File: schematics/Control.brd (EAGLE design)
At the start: 100 x 99.8 mm, 57 parts, among them IC1 THAT1646, IC2 THAT1646, IC5 NE5532N

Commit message: rev01 for pcbtrain express fab
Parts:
- removed BOOT, BOOT1, JP4: (no value), SparkFun:1X03
- removed C501, C502: 2n7 C0G, Rebel:C0603
- removed C503, C504: 100n, Rebel:C0603
- removed JP2: (no value), SparkFun:1X02
- added C10, C300, C301, C9: 0.1uF, capacitor-wima:C5B3.5
- added C11, C12, C610: 100n, rcl:C050-025X075
- added C13, C14: 2n7 C0G, rcl:C050-025X075
- added C15, C16, C611: 100uF, rcl:E2,5-7
- added IN2: (no value), SparkFun:1X02
- added J4, J5: NEUTRIK_NMJ6HCD2, neutrik_jacks:NMJ6HCD2
- added JP13: (no value), SparkFun:1X05
- added R1, R2, R3, R4, R5: 91R, Rebel:0204/7
- added R300, R301: 2M, Rebel:0204/7
- added U$1, U$3, U$4, U$5, U$6: (no value), holes:2,8
- added UART: (no value), SparkFun:1X03
- JP1: device SparkFun:1X02 -> SparkFun:1X05
- R501, R502, R503, R504, R505, R506, R507, R508, R509, R510: device Rebel:0603 -> Rebel:0204/7
- moved C7 210.8 mm to (97.8, 62.2), turned to 180 degrees
- moved RIGHT 209.6 mm to (97.8, 102.9)
- moved C6 207.6 mm to (101.6, 52.1), turned to 90 degrees
- moved C8 203.8 mm to (88.9, 62.2), turned to 180 degrees
- moved C5 196.6 mm to (83.8, 44.5), turned to 270 degrees
- moved IC2 196.5 mm to (94.0, 50.8), turned to 270 degrees
- moved C1 187.5 mm to (101.6, 44.5), turned to 270 degrees
- moved C3 187.2 mm to (80.0, 62.2), turned to 180 degrees
- moved C4 182.4 mm to (71.1, 62.2)
- moved C2 182.1 mm to (83.8, 52.1), turned to 90 degrees
- moved LEFT 160.7 mm to (69.8, 102.9)
- moved IC1 139.4 mm to (76.2, 50.8), turned to 270 degrees
- moved IN1 131.7 mm to (2.86, 21.9), turned to 90 degrees
- moved VMID1 128.1 mm to (2.86, 27.0), turned to 180 degrees
- moved HP1 125.2 mm to (2.86, 32.1), turned to 270 degrees
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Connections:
- removed net +3V3: BOOT.3, BOOT1.3, JP3.3, JP4.3, JP5.3
- removed net AINA: C501.1, R503.2
- removed net AINB: C502.1, R508.2
- removed net BOOT0: BOOT.2, BOOT1.2, JP12.2, JP9.2
- removed net INL: R502.1
- removed net INR: R507.1
- removed net L_IN1: IN.1
- removed net L_IN2: IN1.1
- removed net L_OUT1: HP.2
- removed net L_OUT2: HP1.2
- removed net OUT_LEFT: IC1.4
- removed net OUT_RIGHT: IC2.4
- removed net R_IN1: IN.2
- removed net R_IN2: IN1.2
- removed net R_OUT1: HP.1
- removed net R_OUT2: HP1.1
- removed net USB_VBUS: JP1.2, JP2.2, USB.4, USB1.4
- new net ADC1_A: ADC.4
- new net ADC2_A: ADC.3
- new net ADC3_A: ADC.2
- new net ADC4_A: ADC.1
- new net FX_IN_L: C300.2, J4.T, J5.TN, R300.2
- new net FX_IN_R: C301.2, J5.T, R301.2
- new net L_IN_A: IN.1, R1.1
- new net L_IN_B: C13.1, IN1.1, R503.2
- new net L_OUT_A: C10.2, HP.2
- new net L_OUT_B: HP1.2, R1.2
- new net N$26: C300.1, R502.1
- new net N$30: C301.1, R507.1
- new net N$7: C9.1, IC2.4
- new net N$9: C10.1, IC1.4
- new net PA2_A: JP7.2
- new net PA3_A: JP7.1
- new net PB6_A: JP9.4
- new net PB7_A: JP9.3
- new net PE2_A: JP10.4
- new net PE3_A: JP10.3
- new net PE4_A: JP10.2
- new net PE5_A: JP10.1
- new net PG14_A: JP9.1
- new net RX: R3.1, UART.3
- new net RX_A: JP13.2, R5.1
- new net RX_B: JP1.2, R3.2
- new net R_IN_A: IN.2, R2.1
- new net R_IN_B: C14.1, IN1.2, R508.2
- new net R_OUT_A: C9.2, HP.1
- new net R_OUT_B: HP1.1, R2.2
- new net TX: R4.1, UART.1
- new net TX_A: JP13.3, R4.2
- new net TX_B: JP1.3, R5.2
- new net USB_DM_A: USB.3
- new net USB_DP_A: USB.2
- new net USB_ID_A: USB.1
- net +12V: now also C11.1; no longer C503.1
- net +5V: now also C15.+, C16.+; no longer JP1.1, JP2.1, JP4.1
- net -12V: now also C12.1; no longer C504.1
- net ADC1: no longer ADC.4
- net ADC2: no longer ADC.3
- net ADC3: no longer ADC.2
- net ADC4: no longer ADC.1
- net CS_VREF: now also C13.2, C14.2, C610.1, C611.+, VMID1.1; no longer C501.2, C502.2
- net GND: now also C11.2, C12.2, C15.-, C16.-, C610.2, C611.-, IN2.2, J4.S, J4.TN, J5.S, JP12.2, JP9.2, R300.1, R301.1, UART.2; no longer BOOT.1, BOOT1.1, C503.2, C504.2, JP4.2
- net GNDA: now also IN2.1
- net PA2: no longer JP7.2
- net PA3: no longer JP7.1
- net PB6: no longer JP9.4
- net PB7: no longer JP9.3
- net PE2: no longer JP10.4
- net PE3: no longer JP10.3
- net PE4: no longer JP10.2
- net PE5: no longer JP10.1
- net PG14: no longer JP9.1
- net USB_DM: no longer USB.3
- net USB_DP: no longer USB.2
- net USB_ID: no longer USB.1
- net VCC/2: no longer VMID1.1
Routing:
- net +5V: track 0.00 -> 183.9 mm, vias 0 -> 1
- net +12V: track 0.00 -> 104.5 mm
- net -12V: track 0.00 -> 102.7 mm, vias 0 -> 1
- net TX_A: track 0.00 -> 85.2 mm
- net CS_VREF: track 0.00 -> 84.1 mm, vias 0 -> 3
- net RX_A: track 0.00 -> 72.5 mm
- net R_IN_B: track 0.00 -> 67.0 mm, vias 0 -> 1
- net FX_IN_L: track 0.00 -> 58.9 mm
- net N$3: track 0.00 -> 55.1 mm
- net TX: track 0.00 -> 46.5 mm
- net RX: track 0.00 -> 46.5 mm
- net N$2: track 0.00 -> 44.8 mm
- net L_IN_B: track 0.00 -> 43.0 mm, vias 0 -> 1
- net R_IN_A: track 0.00 -> 42.9 mm
- net N$19: track 0.00 -> 42.9 mm
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- added copper zone on layer 16, net GNDA
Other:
- board size 100 x 99.8 mm -> 115.3 x 90.9 mm
- board text added: "OWL Rack Rev01"
- board text removed: "OWL Modular Rev02"

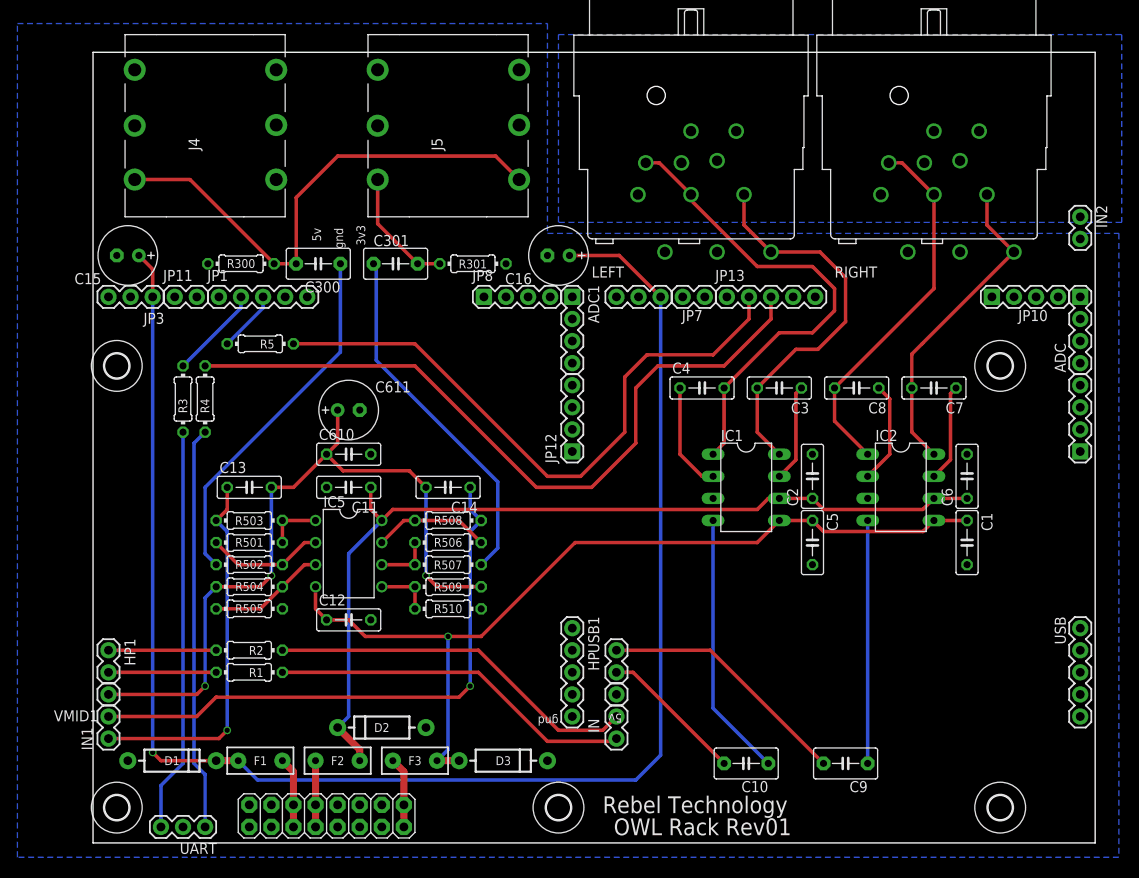
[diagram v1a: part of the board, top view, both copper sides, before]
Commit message: added +5v reg, change power connection, reduced board size
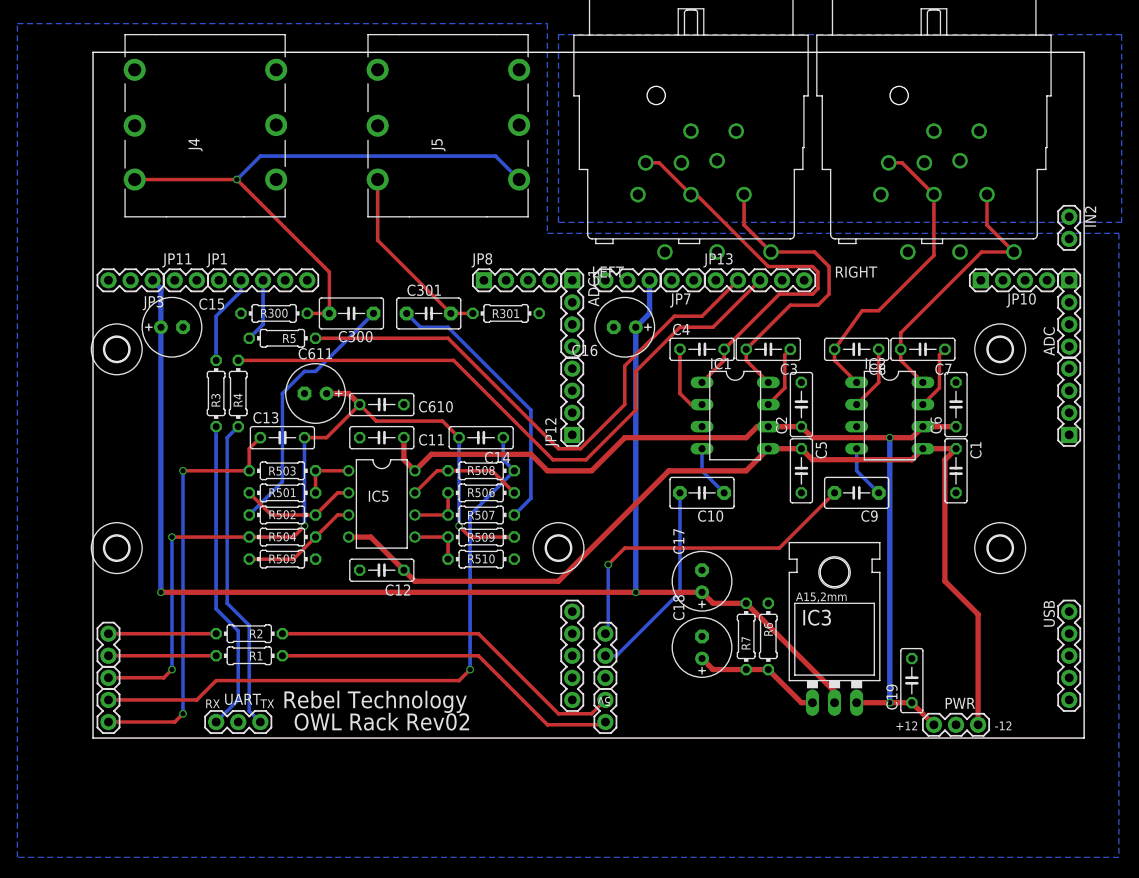
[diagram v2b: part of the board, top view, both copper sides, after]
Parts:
- removed D1, D2, D3: (no value), Rebel:DIODE-1N4001
- removed F1, F2, F3: PTCPTH, Rebel:PTC
- removed U$2: M08X2, SparkFun:2X8
- added C17, C18: 1u, rcl:E2,5-7
- added C19: 100n, rcl:C050-025X075
- added IC3: LM317MABT, v-reg:TO220L1
- added PWR: (no value), SparkFun:1X03
- added R6: 1k, Rebel:0204/7
- added R7: 330R, Rebel:0204/7
- C15, C16: value 100uF -> 100u
- R300, R301: value 2M -> 1M
- moved C10 31.5 mm to (71.1, 50.2)
- moved C9 31.1 mm to (88.9, 50.2)
- moved U$1 29.8 mm to (54.6, 43.8)
- moved U$3 29.8 mm to (105.4, 43.8)
- moved U$4 29.8 mm to (3.81, 43.8)
- moved UART 13.6 mm to (20.3, 23.8)
- moved C16 11.2 mm to (62.2, 69.2)
- moved C15 9.69 mm to (10.2, 69.2), turned to 0 degrees
- moved IC2 8.35 mm to (92.7, 59.1)
- moved C2 8.35 mm to (82.5, 60.3)
- moved C6 8.35 mm to (100.3, 60.3)
- moved IC1 8.35 mm to (74.9, 59.1)
- moved C1 8.35 mm to (100.3, 52.7)
- moved C5 8.35 mm to (82.5, 52.7)
- moved C14 6.87 mm to (45.7, 56.5)
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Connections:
- removed net N$44: F1.P$1, U$2.11, U$2.12
- removed net N$45: F2.P$1, U$2.10, U$2.9
- removed net N$6: F3.P$2, U$2.1, U$2.2
- new net N$11: C18.+, IC3.1, R6.2, R7.1
- net +12V: now also C19.1, IC3.3, PWR.1; no longer D2.C, F2.P$2
- net +5V: now also C17.+, IC3.2, R7.2; no longer D1.C, F1.P$2
- net -12V: now also PWR.3; no longer D3.A, F3.P$1
- net GND: now also C17.-, C18.-, C19.2, PWR.2, R6.1; no longer D1.A, D2.A, D3.C, U$2.3, U$2.4, U$2.5, U$2.6, U$2.7, U$2.8
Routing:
- net +5V: track 183.9 -> 156.3 mm, vias 1 -> 2
- net N$9: track 30.6 -> 6.13 mm
- net N$7: track 27.9 -> 6.13 mm
- net N$11: track 0.00 -> 14.8 mm
- net N$26: track 41.6 -> 29.8 mm
- net -12V: track 102.7 -> 113.2 mm, vias 1 -> 0
- net RX: track 46.5 -> 36.1 mm
- net TX: track 46.5 -> 36.1 mm
- net FX_IN_L: track 58.9 -> 68.8 mm, vias 0 -> 1
- net N$3: track 55.1 -> 45.5 mm
- net N$30: track 41.3 -> 31.7 mm
- net N$2: track 44.8 -> 35.4 mm
- net TX_A: track 85.2 -> 75.9 mm
- net R_OUT_A: track 29.2 -> 37.5 mm, vias 0 -> 1
- net N$44: track 8.15 -> 0.00 mm
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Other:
- board size 115.3 x 90.9 mm -> 114 x 78.9 mm
- board text added: "+12"
- board text added: "-12"
- board text added: "OWL Rack Rev02"
- board text added: "RX"
- board text added: "TX"
- board text removed: "3v3"
- board text removed: "OWL Rack Rev01"
- board text removed: "gnd"

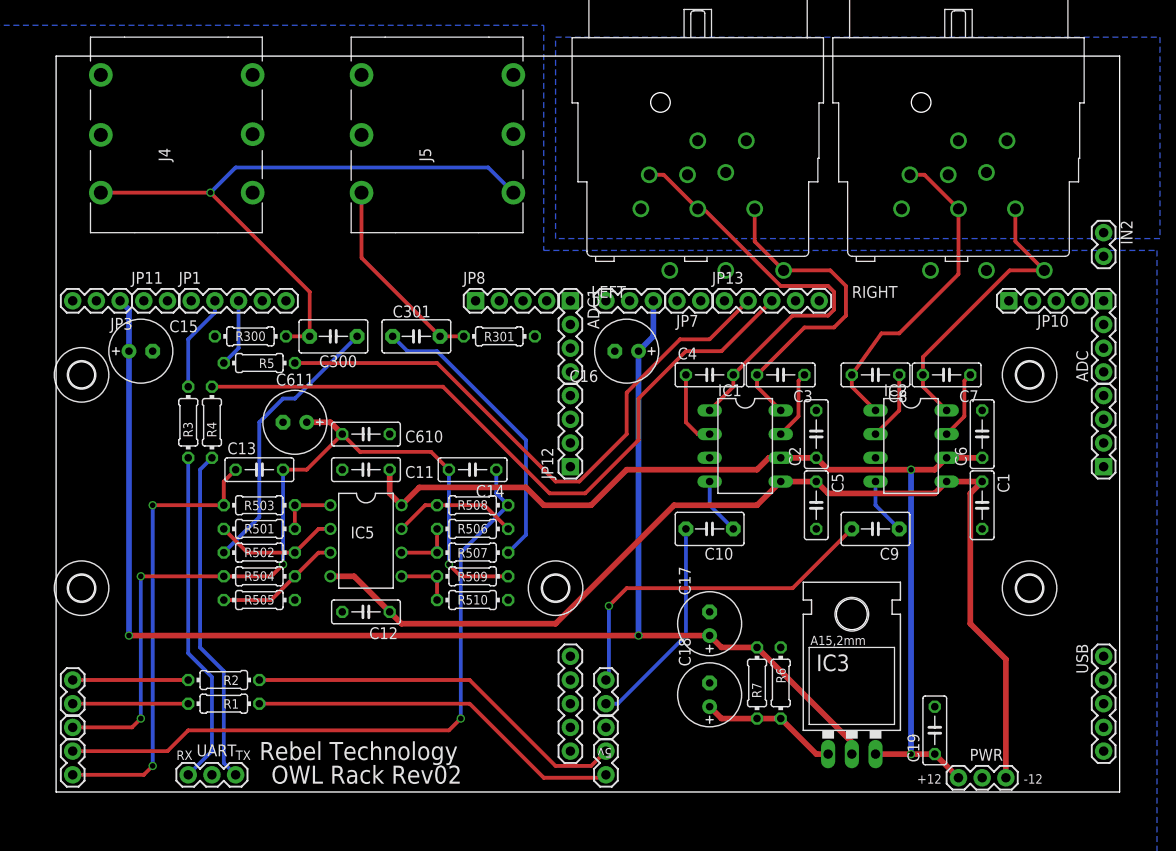
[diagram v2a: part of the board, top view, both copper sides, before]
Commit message: added usb connections and adjusted audio input circuit
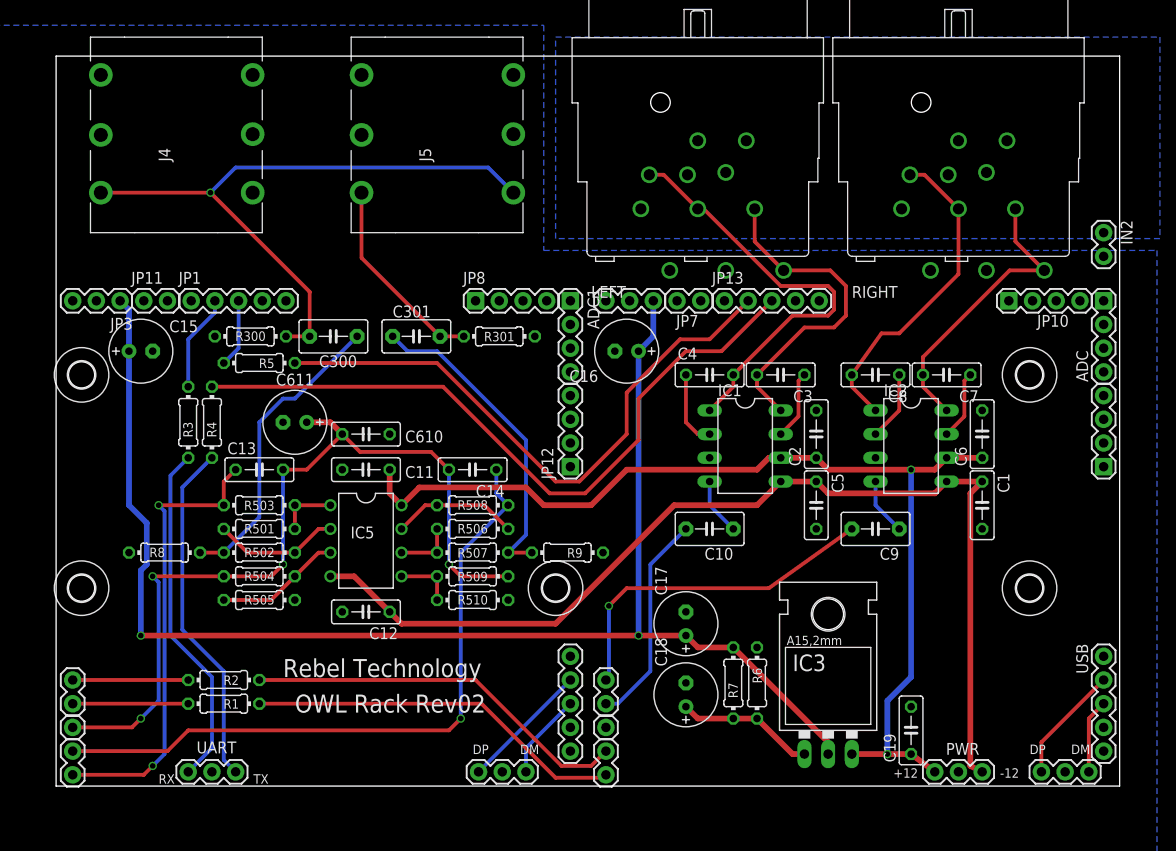
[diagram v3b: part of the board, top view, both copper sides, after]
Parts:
- added R8, R9: 1M, Rebel:0204/7
- added USBA, USBB: (no value), SparkFun:1X03
- R501, R504, R506, R509: value 20k -> 10k
- R502, R505, R507, R510: value 100k -> 10k
- moved PWR 2.62 mm to (95.2, 24.1)
- moved C17 2.54 mm to (68.6, 40.0)
- moved C18 2.54 mm to (68.6, 32.4)
- moved C19 2.54 mm to (92.7, 28.6)
- moved IC3 2.54 mm to (83.8, 29.8)
- moved R7 2.54 mm to (73.7, 33.7)
- moved R6 2.54 mm to (76.2, 33.7)
- moved UART 0.32 mm to (20.3, 24.1)
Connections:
- net USB_ID renamed USB_ID_B
- removed net USB_DM: USB1.3
- removed net USB_DP: USB1.2
- new net USB_DM_B: USB1.3, USBB.3
- new net USB_DP_B: USB1.2, USBB.1
- net GND: now also R8.1, R9.1, USBA.2, USBB.2
- net N$26: now also R8.2
- net N$30: now also R9.2
- net USB_DM_A: now also USBA.3
- net USB_DP_A: now also USBA.1
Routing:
- net USB_DP_B: track 0.00 -> 13.9 mm
- net USB_DP_A: track 0.00 -> 12.6 mm
- net USB_DM_B: track 0.00 -> 9.28 mm
- net USB_DM_A: track 0.00 -> 7.96 mm
- net +5V: track 156.3 -> 153.5 mm
- net N$30: track 31.7 -> 34.3 mm
- net N$26: track 29.8 -> 32.4 mm
- net -12V: track 113.2 -> 111.7 mm
- net RX: track 36.1 -> 37.3 mm
- net TX: track 36.1 -> 37.3 mm
- net +12V: track 111.7 -> 112.4 mm
- net R_OUT_A: track 37.5 -> 36.9 mm
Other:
- board size 114 x 78.9 mm -> 114 x 78.2 mm
- board text added: "DM"
- board text added: "DP"
- board text removed: "5v"
